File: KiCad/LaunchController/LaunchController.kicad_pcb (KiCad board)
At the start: 2 copper layers, 120 x 86 mm, 123 parts, among them J1 DC_IN, J10 RJ45, J13 TO_CONVERTER, J14 FROM_CONVERTER, J17 CONN_STATUS_PANEL, J2 CONN_USB, J22 CONN_PANEL_BAORD_2, J23 CONN_PANEL_BAORD_1, J3 USB_B_Micro, J4 CONN_AUDIO, J5 CONN_SPEAKER, J6 CONN_ICSP, Q1 TJ8S06M3L, Q2 2SC3325-Y, Q3 TJ8S06M3L, SW1 SW_RESET, U1 FT232RL, U11 DFPlayer, U2 24LC256, U3 INA219BIDCNT, U4 ATMEGA2560-16AUR, U5 INA219BIDCNT, U6 NJM7805SDL1, U7 LTC485CN8#PBF, Y1 HUSG-16.000-20

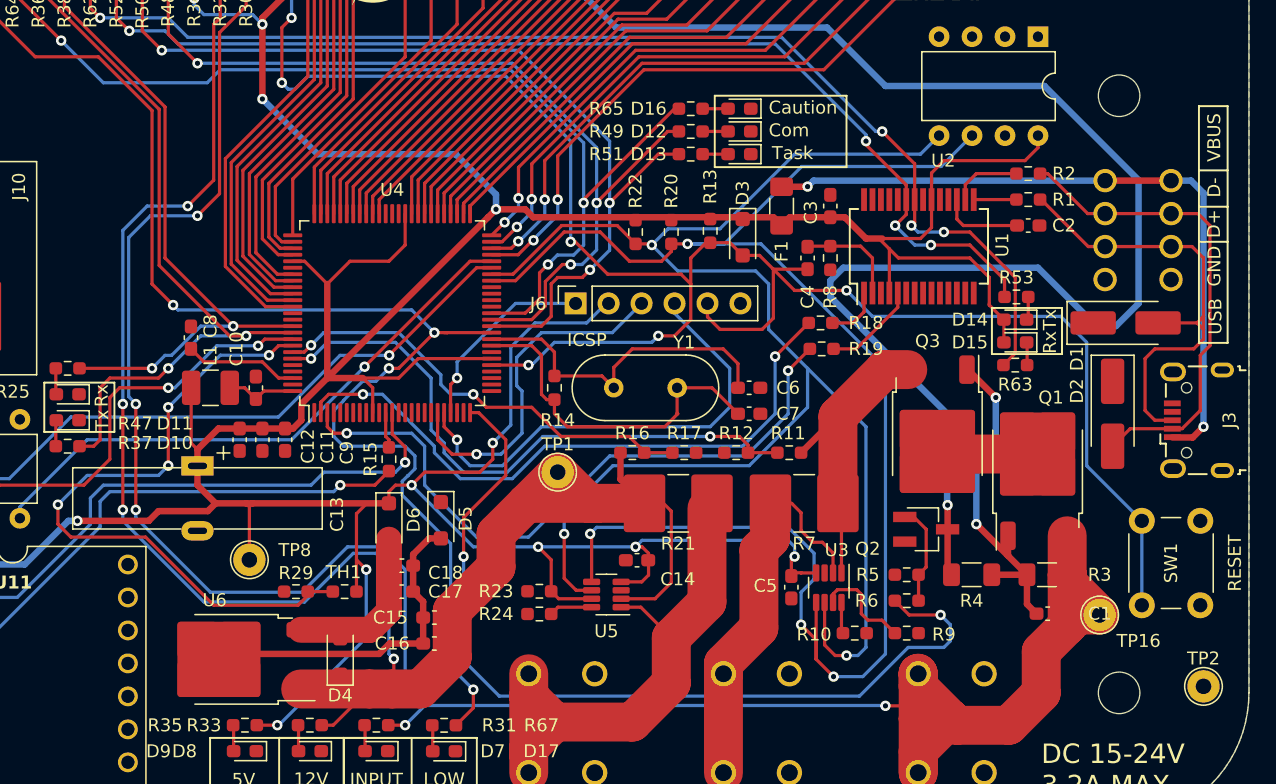
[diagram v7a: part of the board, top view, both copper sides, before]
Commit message: 🚧 隠れいらない配線を修正しています．
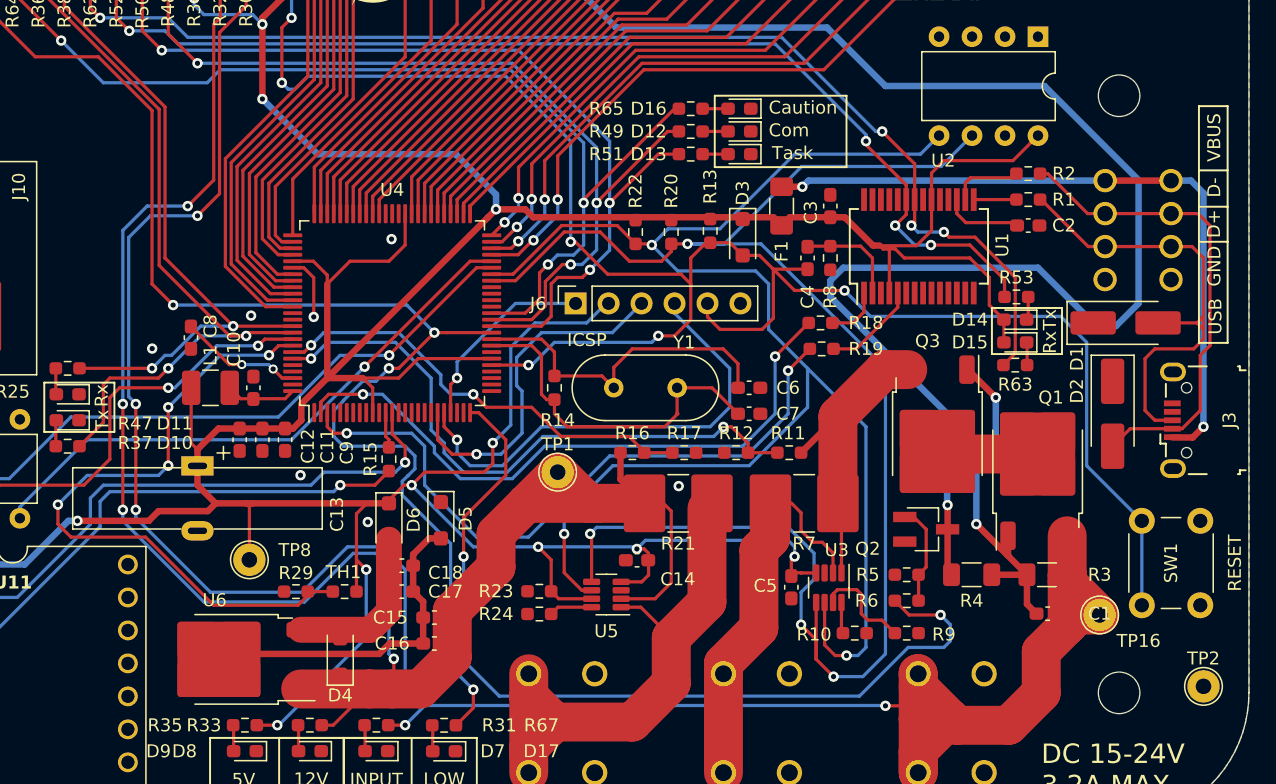
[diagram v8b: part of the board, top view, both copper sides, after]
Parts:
- moved C10 0.19 mm to (117.5, 100.5)
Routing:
- net USB_GND: track 0.00 -> 4.96 mm, vias 0 -> 7
- net FROM_CONVERTER: track 45.0 -> 43.4 mm
- net LED_INPUT: track 174.2 -> 173.2 mm
- net LED_5V: track 429.9 -> 429.0 mm
- net Net-(U4-AREF): track 8.77 -> 9.48 mm, vias 0 -> 2
- net VREF_VSW: track 46.8 -> 47.5 mm
- net LED_RS485_TX: track 57.5 -> 56.9 mm
- net SPI_MOSI: track 37.1 -> 36.5 mm
